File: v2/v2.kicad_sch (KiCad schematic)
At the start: 65 parts, among them J1 cBUSoutV, J10 mcuTIEout, J2 cBUSinV, J3 cTIEoutV, J4 cTIEinV, J5 rBUSoutH, J6 cTIEoutH, J7 mcuTIEin, J8 cTIEinH, J9 rBUSinH, SW1 KeySwitch, SW10 KeySwitch, SW11 KeySwitch, SW12 KeySwitch, SW13 KeySwitch, SW14 KeySwitch, SW15 KeySwitch, SW16 KeySwitch, SW17 KeySwitch, SW18 KeySwitch, SW19 KeySwitch, SW2 KeySwitch, SW20 KeySwitch, SW21 KeySwitch, SW22 KeySwitch, SW23 KeySwitch, SW24 KeySwitch, SW25 KeySwitch, SW3 KeySwitch, SW4 KeySwitch, SW5 KeySwitch, SW6 KeySwitch, SW7 KeySwitch, SW8 KeySwitch, SW9 KeySwitch, U1 ItsyBitsy5V

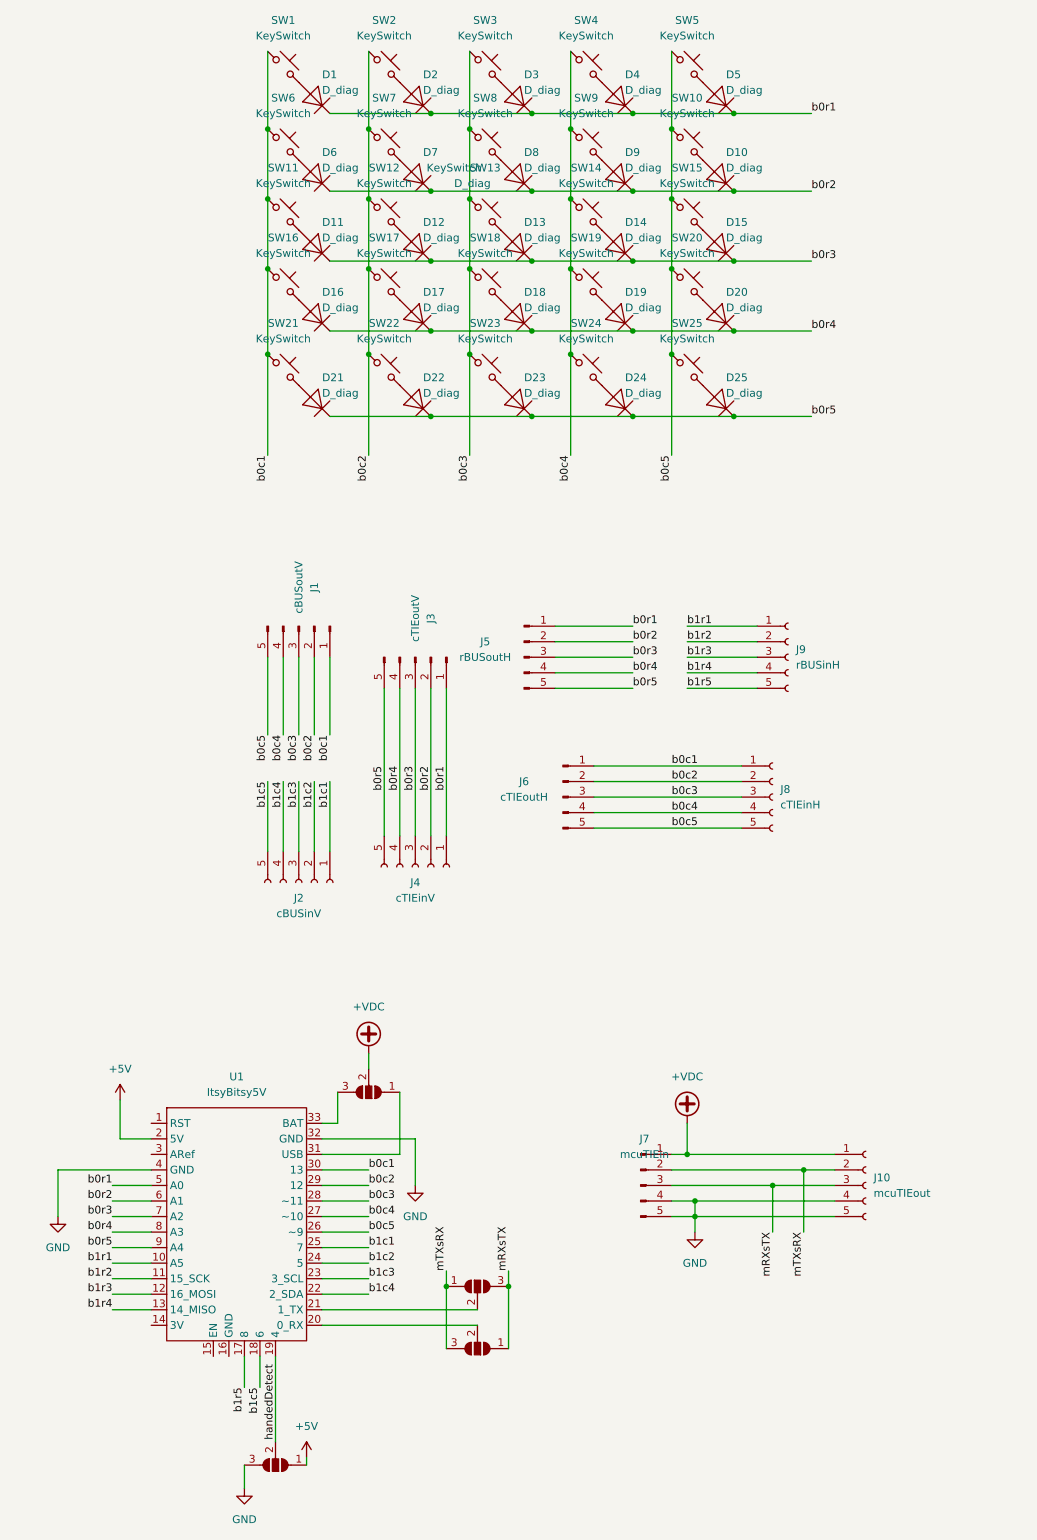
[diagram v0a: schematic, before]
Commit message: Refactor to include USB
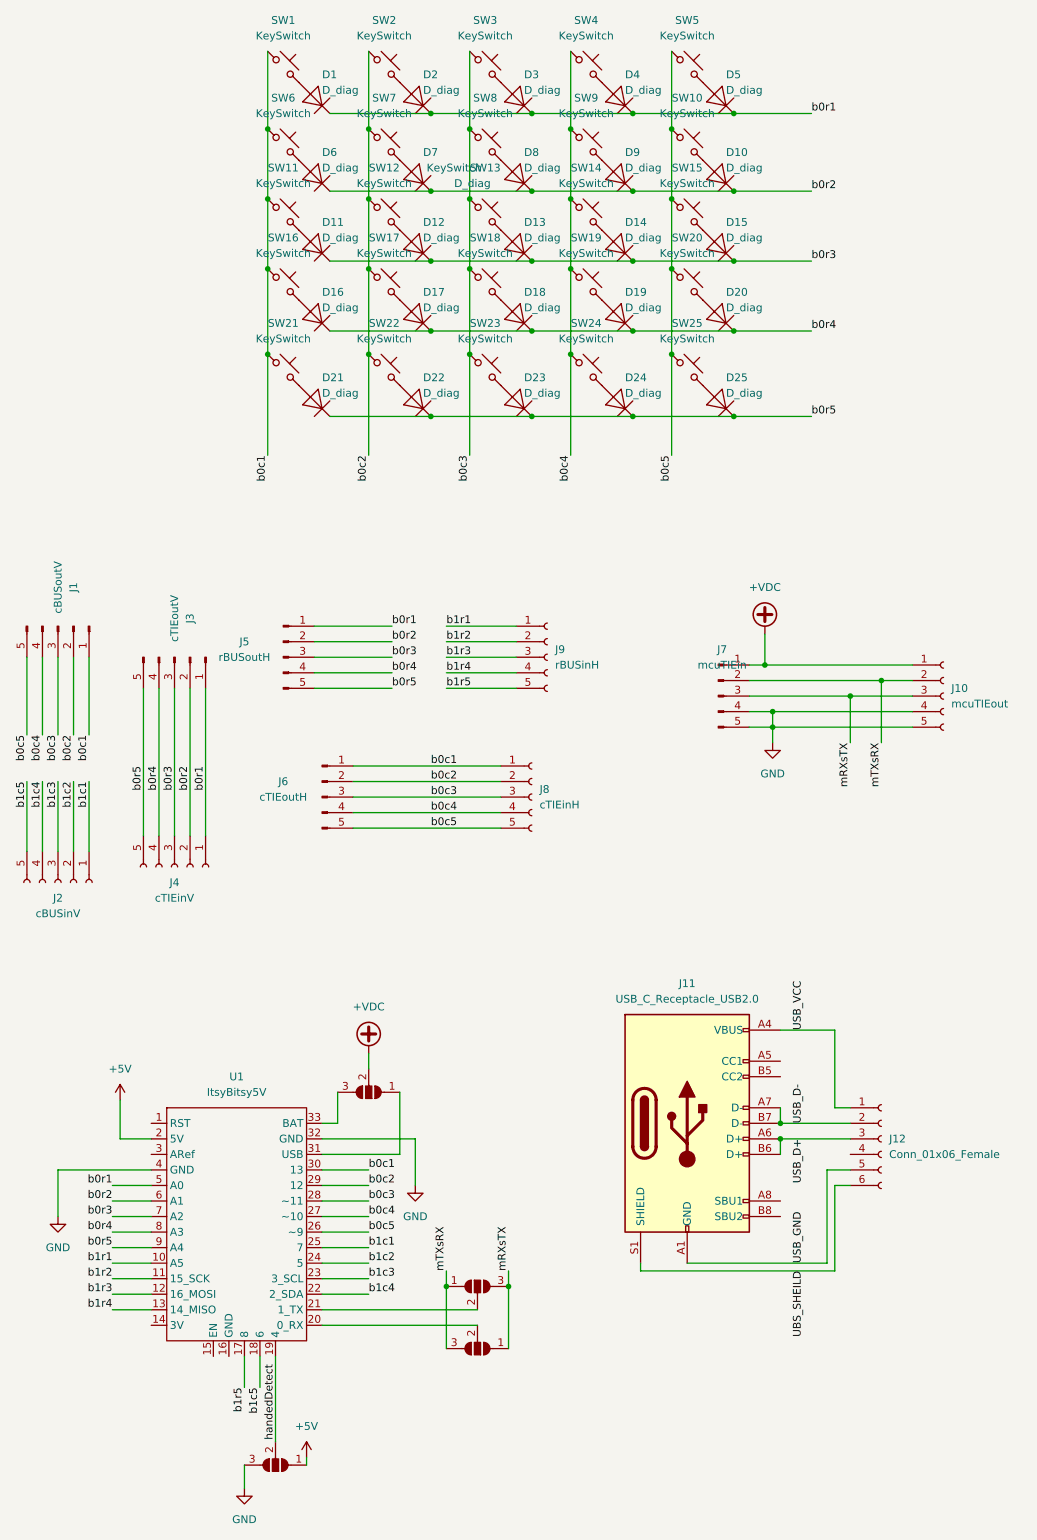
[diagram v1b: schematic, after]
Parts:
- added J11: USB_C_Receptacle_USB2.0, Connector_USB:USB_C_Receptacle_XKB_U262-16XN-4BVC11, symbol Connector:USB_C_Receptacle_USB2.0
- added J12: Conn_01x06_Female, ProjectLibrary:USB_JUMP_PAD, symbol Connector:Conn_01x06_Female
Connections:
- new net UBS_SHEILD: J11.S1 (SHIELD), J12.6 (Pin_6)
- new net USB_D+: J11.A6 (D+), J11.B6 (D+), J12.3 (Pin_3)
- new net USB_D-: J11.A7 (D-), J11.B7 (D-), J12.2 (Pin_2)
- new net USB_GND: J11.A1 (GND), J11.A12 (GND), J11.B1 (GND), J11.B12 (GND), J12.5 (Pin_5)
- new net USB_VCC: J11.A4 (VBUS), J11.A9 (VBUS), J11.B4 (VBUS), J11.B9 (VBUS), J12.1 (Pin_1)
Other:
- moved on the sheet: J1, J10, J2, J3, J4, J5, J6, J7, J8, J9

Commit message: Fix connection error in BUSs & TIEs
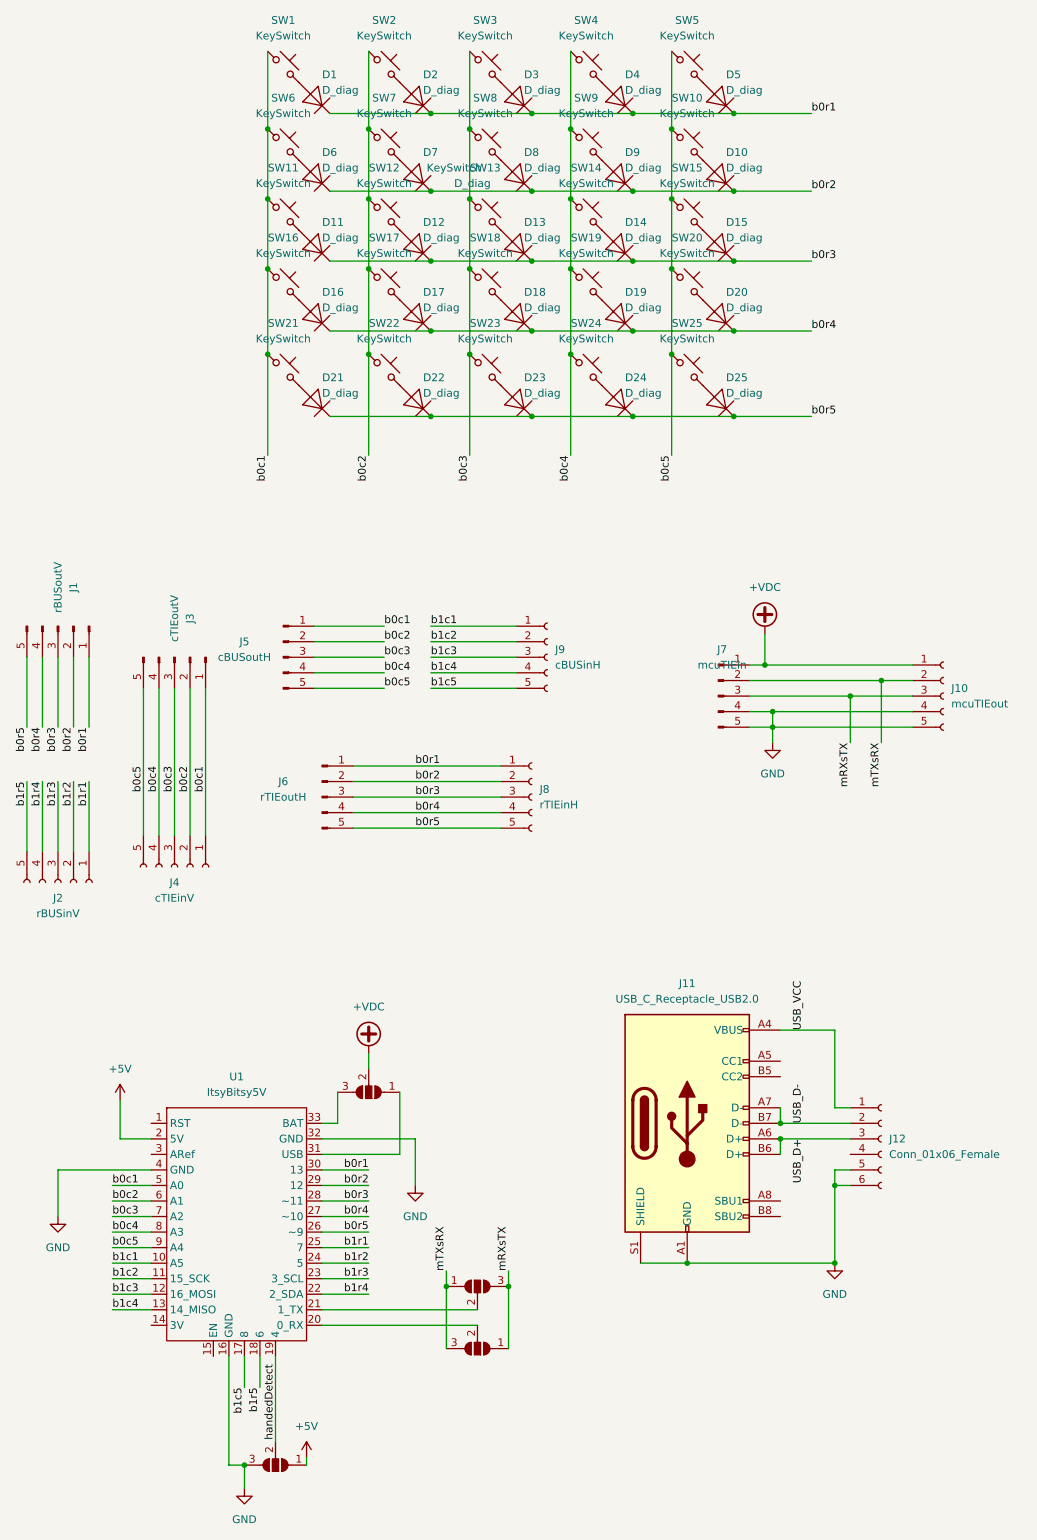
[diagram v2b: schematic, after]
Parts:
- J1: value cBUSoutV -> rBUSoutV
- J11: footprint Connector_USB:USB_C_Receptacle_XKB_U262-16XN-4BVC11 -> ProjectLibrary:USB_C_Receptacle_XKB_U262-16XN-4BVC11_NoSilk
- J2: value cBUSinV -> rBUSinV
- J5: value rBUSoutH -> cBUSoutH
- J6: value cTIEoutH -> rTIEoutH
- J8: value cTIEinH -> rTIEinH
- J9: value rBUSinH -> cBUSinH
- JP1, JP2, JP3, JP4: footprint Jumper:SolderJumper-3_P1.3mm_Open_RoundedPad1.0x1.5mm -> ProjectLibrary:SolderJumper-3_P1.3mm_Open_RoundedPad1.0x1.5mm_No_Silk
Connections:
- net UBS_SHEILD is gone; now on net GND: J11.S1 (SHIELD), J12.6 (Pin_6)
- net USB_GND is gone; now on net GND: J11.A1 (GND), J11.A12 (GND), J11.B1 (GND), J11.B12 (GND), J12.5 (Pin_5)
- net GND: now also U1.16 (GND)
- net b0c1: now also J3.1 (Pin_1), J4.1 (Pin_1), J5.1 (Pin_1), U1.5 (A0); no longer J1.1 (Pin_1), J6.1 (Pin_1), J8.1 (Pin_1), U1.30 (13)
- net b0c2: now also J3.2 (Pin_2), J4.2 (Pin_2), J5.2 (Pin_2), U1.6 (A1); no longer J1.2 (Pin_2), J6.2 (Pin_2), J8.2 (Pin_2), U1.29 (12)
- net b0c3: now also J3.3 (Pin_3), J4.3 (Pin_3), J5.3 (Pin_3), U1.7 (A2); no longer J1.3 (Pin_3), J6.3 (Pin_3), J8.3 (Pin_3), U1.28 (~11)
- net b0c4: now also J3.4 (Pin_4), J4.4 (Pin_4), J5.4 (Pin_4), U1.8 (A3); no longer J1.4 (Pin_4), J6.4 (Pin_4), J8.4 (Pin_4), U1.27 (~10)
- net b0c5: now also J3.5 (Pin_5), J4.5 (Pin_5), J5.5 (Pin_5), U1.9 (A4); no longer J1.5 (Pin_5), J6.5 (Pin_5), J8.5 (Pin_5), U1.26 (~9)
- net b0r1: now also J1.1 (Pin_1), J6.1 (Pin_1), J8.1 (Pin_1), U1.30 (13); no longer J3.1 (Pin_1), J4.1 (Pin_1), J5.1 (Pin_1), U1.5 (A0)
- net b0r2: now also J1.2 (Pin_2), J6.2 (Pin_2), J8.2 (Pin_2), U1.29 (12); no longer J3.2 (Pin_2), J4.2 (Pin_2), J5.2 (Pin_2), U1.6 (A1)
- net b0r3: now also J1.3 (Pin_3), J6.3 (Pin_3), J8.3 (Pin_3), U1.28 (~11); no longer J3.3 (Pin_3), J4.3 (Pin_3), J5.3 (Pin_3), U1.7 (A2)
- net b0r4: now also J1.4 (Pin_4), J6.4 (Pin_4), J8.4 (Pin_4), U1.27 (~10); no longer J3.4 (Pin_4), J4.4 (Pin_4), J5.4 (Pin_4), U1.8 (A3)
- net b0r5: now also J1.5 (Pin_5), J6.5 (Pin_5), J8.5 (Pin_5), U1.26 (~9); no longer J3.5 (Pin_5), J4.5 (Pin_5), J5.5 (Pin_5), U1.9 (A4)
- net b1c1: now also J9.1 (Pin_1), U1.10 (A5); no longer J2.1 (Pin_1), U1.25 (7)
- net b1c2: now also J9.2 (Pin_2), U1.11 (15_SCK); no longer J2.2 (Pin_2), U1.24 (5)
- net b1c3: now also J9.3 (Pin_3), U1.12 (16_MOSI); no longer J2.3 (Pin_3), U1.23 (3_SCL)
- net b1c4: now also J9.4 (Pin_4), U1.13 (14_MISO); no longer J2.4 (Pin_4), U1.22 (2_SDA)
- net b1c5: now also J9.5 (Pin_5), U1.17 (8); no longer J2.5 (Pin_5), U1.18 (6)
- net b1r1: now also J2.1 (Pin_1), U1.25 (7); no longer J9.1 (Pin_1), U1.10 (A5)
- net b1r2: now also J2.2 (Pin_2), U1.24 (5); no longer J9.2 (Pin_2), U1.11 (15_SCK)
- net b1r3: now also J2.3 (Pin_3), U1.23 (3_SCL); no longer J9.3 (Pin_3), U1.12 (16_MOSI)
- net b1r4: now also J2.4 (Pin_4), U1.22 (2_SDA); no longer J9.4 (Pin_4), U1.13 (14_MISO)
- net b1r5: now also J2.5 (Pin_5), U1.18 (6); no longer J9.5 (Pin_5), U1.17 (8)

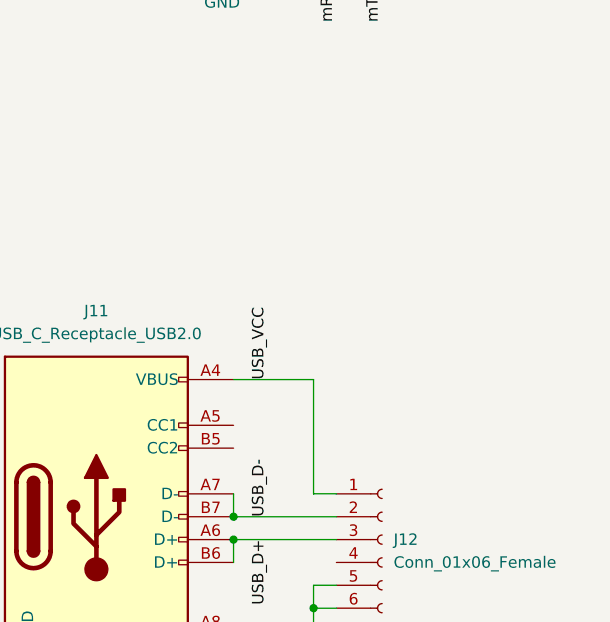
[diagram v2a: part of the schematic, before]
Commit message: Add mounting holes, tweak gound plane
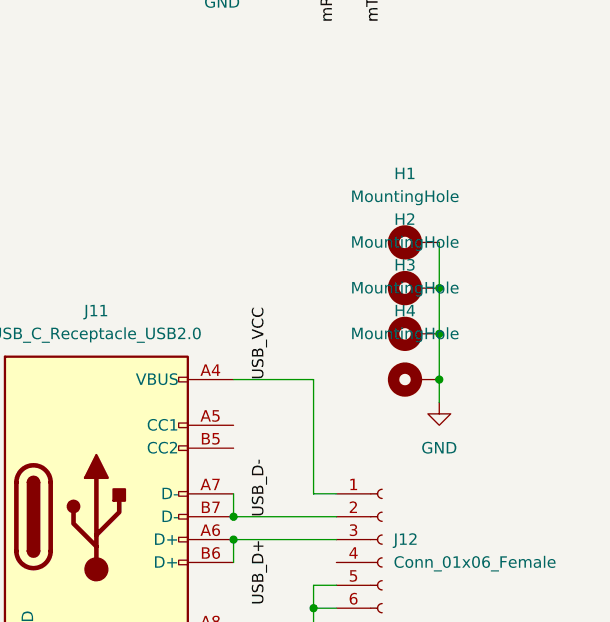
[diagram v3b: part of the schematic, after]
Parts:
- added H1, H2, H3, H4: MountingHole, ProjectLibrary:MountingHole_Screw_2.5mm, symbol Mechanical:MountingHole_Pad
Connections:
- net GND: now also H1.1, H2.1, H3.1, H4.1
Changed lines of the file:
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@@
   (junction (at 157.48 135.89) (diameter 0) (color 0 0 0 0)
   )
+  (junction (at 168.91 180.34) (diameter 0) (color 0 0 0 0)
+  )
   (junction (at 130.81 228.6) (diameter 0) (color 0 0 0 0)
   )
@@
   (junction (at 138.43 76.2) (diameter 0) (color 0 0 0 0)
   )
+  (junction (at 168.91 185.42) (diameter 0) (color 0 0 0 0)
+  )
   (junction (at 78.74 66.04) (diameter 0) (color 0 0 0 0)
   )
@@
   (junction (at 154.94 228.6) (diameter 0) (color 0 0 0 0)
   )
+  (junction (at 168.91 190.5) (diameter 0) (color 0 0 0 0)
+  )
   (junction (at 144.78 138.43) (diameter 0) (color 0 0 0 0)
   )
@@
     (stroke (width 0) (type default) (color 0 0 0 0))
   )
+  (wire (pts (xy 168.91 180.34) (xy 168.91 185.42))
+    (stroke (width 0) (type default) (color 0 0 0 0))
+  )
   (wire (pts (xy 111.76 43.18) (xy 111.76 54.61))
     (stroke (width 0) (type default) (color 0 0 0 0))
@@
     (stroke (width 0) (type default) (color 0 0 0 0))
   )
+  (wire (pts (xy 168.91 190.5) (xy 168.91 193.04))
+    (stroke (width 0) (type default) (color 0 0 0 0))
+  )
   (wire (pts (xy 88.9 127) (xy 102.87 127))
     (stroke (width 0) (type default) (color 0 0 0 0))
@@
     (stroke (width 0) (type default) (color 0 0 0 0))
   )
+  (wire (pts (xy 168.91 175.26) (xy 168.91 180.34))
+    (stroke (width 0) (type default) (color 0 0 0 0))
+  )
   (wire (pts (xy 72.39 76.2) (xy 88.9 76.2))
     (stroke (width 0) (type default) (color 0 0 0 0))
@@
   )
   (wire (pts (xy 157.48 135.89) (xy 167.64 135.89))
+    (stroke (width 0) (type default) (color 0 0 0 0))
+  )
+  (wire (pts (xy 168.91 185.42) (xy 168.91 190.5))
     (stroke (width 0) (type default) (color 0 0 0 0))
   )
@@
     (pin "2")
   )
+  (symbol (lib_id "Mechanical:MountingHole_Pad") (at 166.37 185.42 90) (unit 1)
+    (in_bom yes) (on_board yes) (fields_autoplaced)
+    (property "Reference" "H3" (id 0) (at 165.1 177.8 90))
+    (property "Value" "MountingHole" (id 1) (at 165.1 180.34 90))
+    (property "Footprint" "ProjectLibrary:MountingHole_Screw_2.5mm" (id 2) (at 166.37 185.42 0)
+      (effects (font (size 1.27 1.27)) hide)
+    )
+    (property "Datasheet" "~" (id 3) (at 166.37 185.42 0)
+      (effects (font (size 1.27 1.27)) hide)
+    )
+    (pin "1")
+  )
   (symbol (lib_id "Connector:Conn_01x05_Male") (at 27.94 124.46 270) (unit 1)
     (in_bom yes) (on_board yes)
@@
     (pin "1")
     (pin "2")
+  )
+  (symbol (lib_id "Mechanical:MountingHole_Pad") (at 166.37 180.34 90) (unit 1)
+    (in_bom yes) (on_board yes) (fields_autoplaced)
+    (property "Reference" "H2" (id 0) (at 165.1 172.72 90))
+    (property "Value" "MountingHole" (id 1) (at 165.1 175.26 90))
+    (property "Footprint" "ProjectLibrary:MountingHole_Screw_2.5mm" (id 2) (at 166.37 180.34 0)
+      (effects (font (size 1.27 1.27)) hide)
+    )
+    (property "Datasheet" "~" (id 3) (at 166.37 180.34 0)
+      (effects (font (size 1.27 1.27)) hide)
+    )
+    (pin "1")
   )
   (symbol (lib_id "Jumper:SolderJumper_3_Open") (at 63.5 261.62 180) (unit 1)
@@
     (pin "2")
   )
+  (symbol (lib_id "Mechanical:MountingHole_Pad") (at 166.37 190.5 90) (unit 1)
+    (in_bom yes) (on_board yes) (fields_autoplaced)
+    (property "Reference" "H4" (id 0) (at 165.1 182.88 90))
+    (property "Value" "MountingHole" (id 1) (at 165.1 185.42 90))
+    (property "Footprint" "ProjectLibrary:MountingHole_Screw_2.5mm" (id 2) (at 166.37 190.5 0)
+      (effects (font (size 1.27 1.27)) hide)
+    )
+    (property "Datasheet" "~" (id 3) (at 166.37 190.5 0)
+      (effects (font (size 1.27 1.27)) hide)
+    )
+    (pin "1")
+  )
   (symbol (lib_id "power:GND") (at 154.94 228.6 0) (unit 1)
     (in_bom yes) (on_board yes) (fields_autoplaced)
@@
     (pin "1")
     (pin "2")
+  )
+  (symbol (lib_id "power:GND") (at 168.91 193.04 0) (unit 1)
+    (in_bom yes) (on_board yes) (fields_autoplaced)
+    (property "Reference" "#PWR?" (id 0) (at 168.91 199.39 0)
+      (effects (font (size 1.27 1.27)) hide)
+    )
+    (property "Value" "GND" (id 1) (at 168.91 198.12 0))
+    (property "Footprint" "" (id 2) (at 168.91 193.04 0)
+      (effects (font (size 1.27 1.27)) hide)
+    )
+    (property "Datasheet" "" (id 3) (at 168.91 193.04 0)
+      (effects (font (size 1.27 1.27)) hide)
+    )
+    (pin "1")
   )
   (symbol (lib_id "Connector:Conn_01x05_Female") (at 27.94 166.37 270) (unit 1)
@@
     (pin "1")
     (pin "2")
+  )
+  (symbol (lib_id "Mechanical:MountingHole_Pad") (at 166.37 175.26 90) (unit 1)
+    (in_bom yes) (on_board yes) (fields_autoplaced)
+    (property "Reference" "H1" (id 0) (at 165.1 167.64 90))
+    (property "Value" "MountingHole" (id 1) (at 165.1 170.18 90))
+    (property "Footprint" "ProjectLibrary:MountingHole_Screw_2.5mm" (id 2) (at 166.37 175.26 0)
+      (effects (font (size 1.27 1.27)) hide)
+    )
+    (property "Datasheet" "~" (id 3) (at 166.37 175.26 0)
+      (effects (font (size 1.27 1.27)) hide)
+    )
+    (pin "1")
   )
   (symbol (lib_id "Switch:SW_Push_45deg") (at 81.28 82.55 0) (unit 1)
@@
       (reference "#PWR0109") (unit 1) (value "GND") (footprint "")
     )
+    (path "/6a4bc668-5f4e-4186-b37b-5eaa10d491ba"
+      (reference "#PWR?") (unit 1) (value "GND") (footprint "")
+    )
     (path "/a2dacdd1-67cc-417f-98c0-d837b8a77a7f"
       (reference "D1") (unit 1) (value "D_diag") (footprint "ProjectLibrary:D_SOD-123_NoSilk")
@@
       (reference "D25") (unit 1) (value "D_diag") (footprint "ProjectLibrary:D_SOD-123_NoSilk")
     )
+    (path "/931b2192-b16b-4ebe-b929-3a8ff8451b32"
+      (reference "H1") (unit 1) (value "MountingHole") (footprint "ProjectLibrary:MountingHole_Screw_2.5mm")
+    )
+    (path "/262f85ee-a49a-4194-bdee-29ac02a484ec"
+      (reference "H2") (unit 1) (value "MountingHole") (footprint "ProjectLibrary:MountingHole_Screw_2.5mm")
+    )
+    (path "/1dd3f962-5748-406e-9e93-5433cdf60104"
+      (reference "H3") (unit 1) (value "MountingHole") (footprint "ProjectLibrary:MountingHole_Screw_2.5mm")
+    )
+    (path "/5d09d6c7-c8e2-47a4-9a31-bc7069da0fda"
+      (reference "H4") (unit 1) (value "MountingHole") (footprint "ProjectLibrary:MountingHole_Screw_2.5mm")
+    )
     (path "/1f3f36a5-1f23-42b6-8ea4-7d711f6d3716"
